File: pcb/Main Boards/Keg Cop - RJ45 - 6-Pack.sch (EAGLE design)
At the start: 25 parts

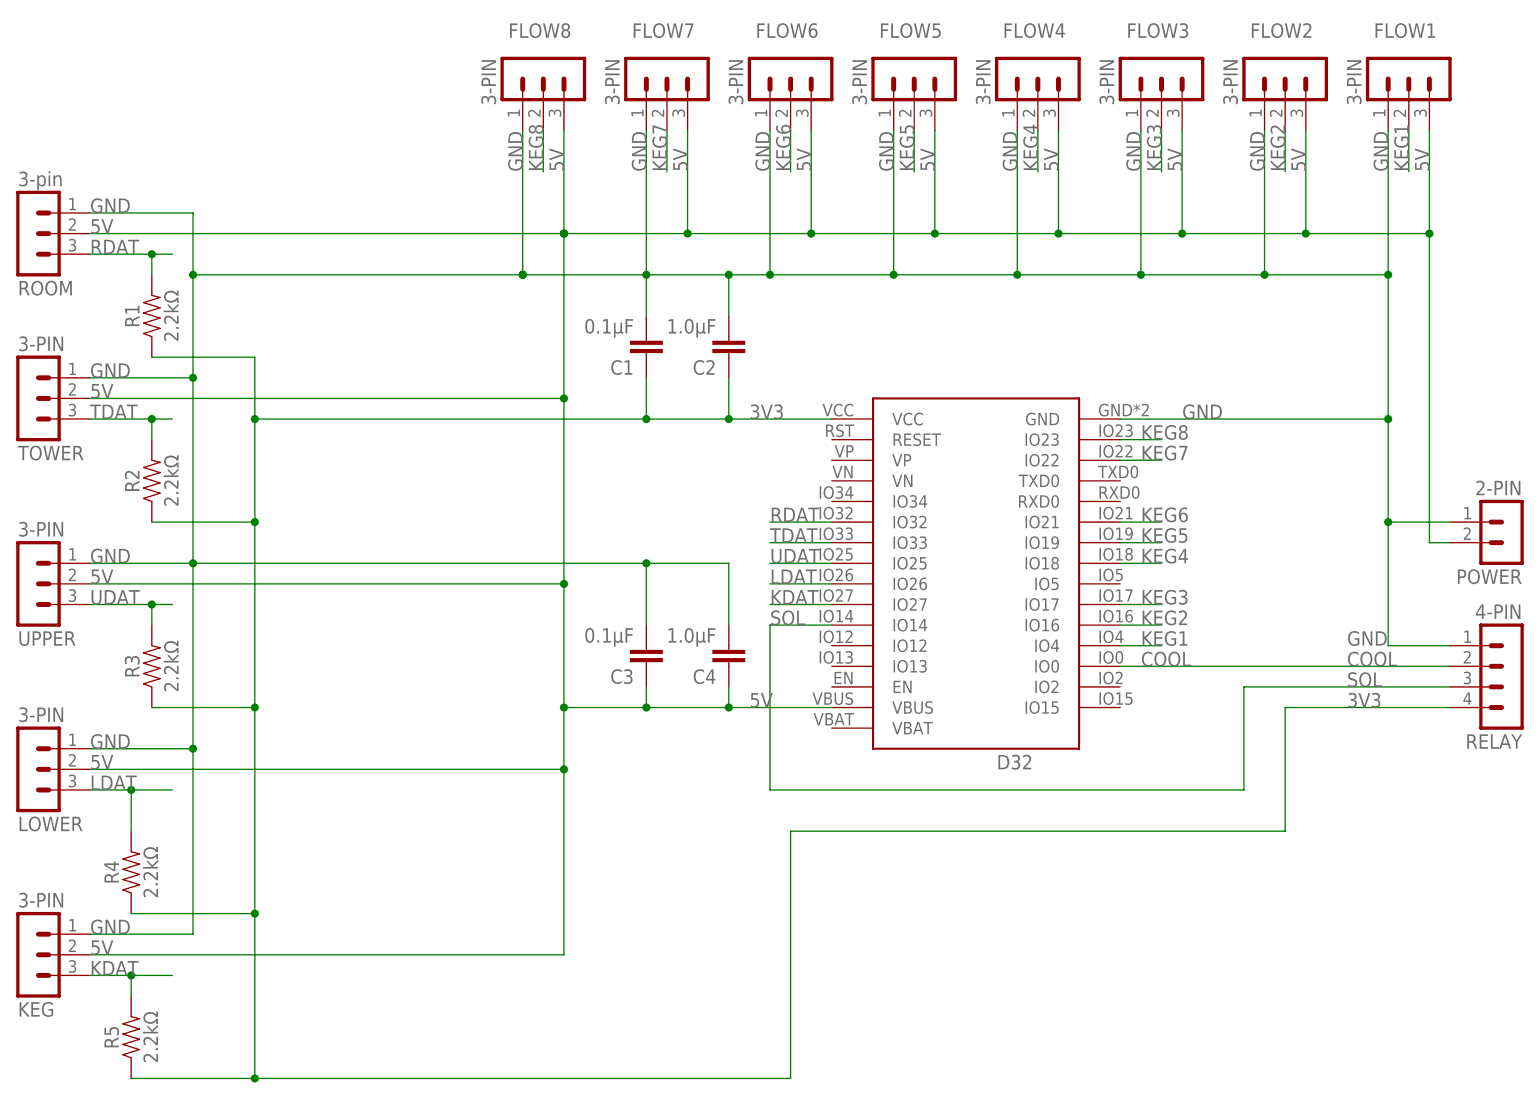
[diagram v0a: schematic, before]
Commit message: Swap pins, split dirs
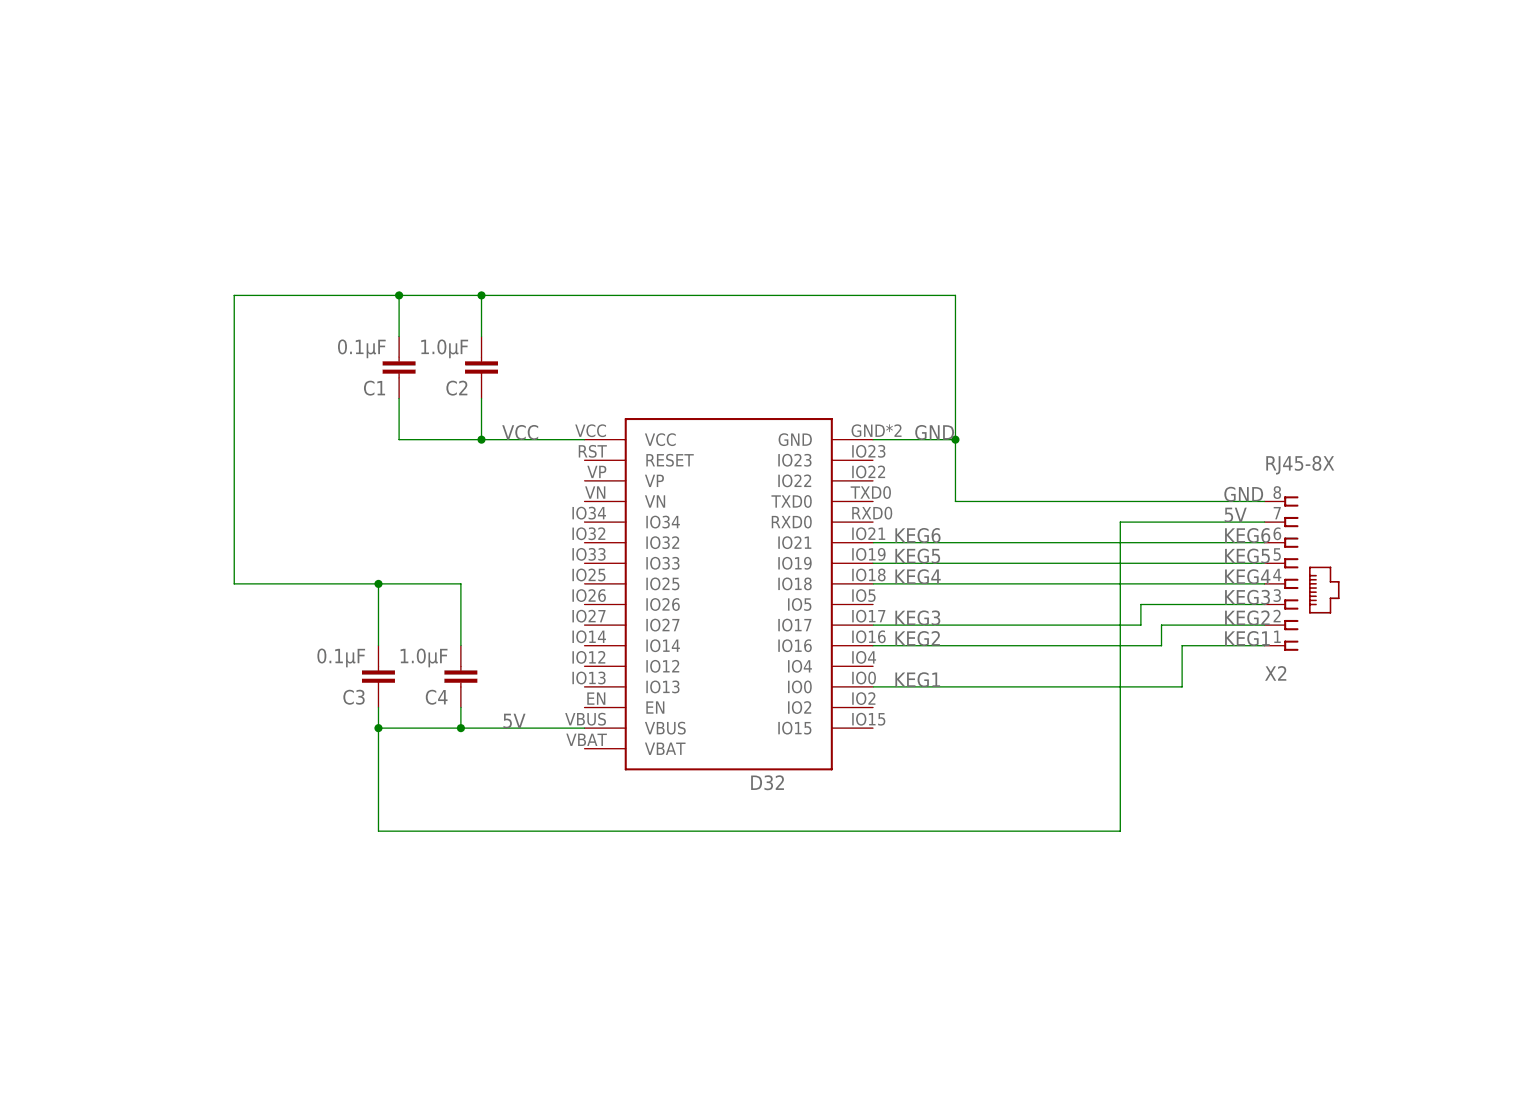
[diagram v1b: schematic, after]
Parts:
- removed FLOW1, FLOW2, FLOW3, FLOW4, FLOW5, FLOW6, FLOW7, FLOW8, KEG, LOWER, TOWER, UPPER: 3-PIN, Donnie:MA03-1
- removed POWER: 2-PIN, Donnie:HDR-2
- removed R1, R2, R3, R4, R5: 2.2kΩ, SparkFun-Resistors:RESISTORAXIAL-0.3
- removed RELAY: 4-PIN, Donnie:MA04-1
- removed ROOM: 3-pin, Donnie:MA03-1
- added X2: RJ45-8X, con-tycoelectronics:RJ45-8X
- D32: value (none) -> Lolin D32
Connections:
- removed net 3V3: C1.1, C2.1, D32.VCC, R1.1, R2.1, R3.1, R4.1, R5.1, RELAY.4
- removed net COOL: D32.IO0, RELAY.2
- removed net KDAT: D32.IO27, KEG.3, R5.2
- removed net KEG7: D32.IO22, FLOW7.2
- removed net KEG8: D32.IO23, FLOW8.2
- removed net LDAT: D32.IO26, LOWER.3, R4.2
- removed net RDAT: D32.IO32, R1.2, ROOM.3
- removed net SOL: D32.IO14, RELAY.3
- removed net TDAT: D32.IO33, R2.2, TOWER.3
- removed net UDAT: D32.IO25, R3.2, UPPER.3
- new net VCC: C1.1, C2.1, D32.VCC
- net 5V: now also X2.7; no longer FLOW1.3, FLOW2.3, FLOW3.3, FLOW4.3, FLOW5.3, FLOW6.3, FLOW7.3, FLOW8.3, KEG.2, LOWER.2, POWER.2, ROOM.2, TOWER.2, UPPER.2
- net GND: now also X2.8; no longer FLOW1.1, FLOW2.1, FLOW3.1, FLOW4.1, FLOW5.1, FLOW6.1, FLOW7.1, FLOW8.1, KEG.1, LOWER.1, POWER.1, RELAY.1, ROOM.1, TOWER.1, UPPER.1
- net KEG1: now also D32.IO0, X2.1; no longer D32.IO4, FLOW1.2
- net KEG2: now also X2.2; no longer FLOW2.2
- net KEG3: now also X2.3; no longer FLOW3.2
- net KEG4: now also X2.4; no longer FLOW4.2
- net KEG5: now also X2.5; no longer FLOW5.2
- net KEG6: now also X2.6; no longer FLOW6.2
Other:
- moved on the sheet: C1, C2, C3, C4, D32

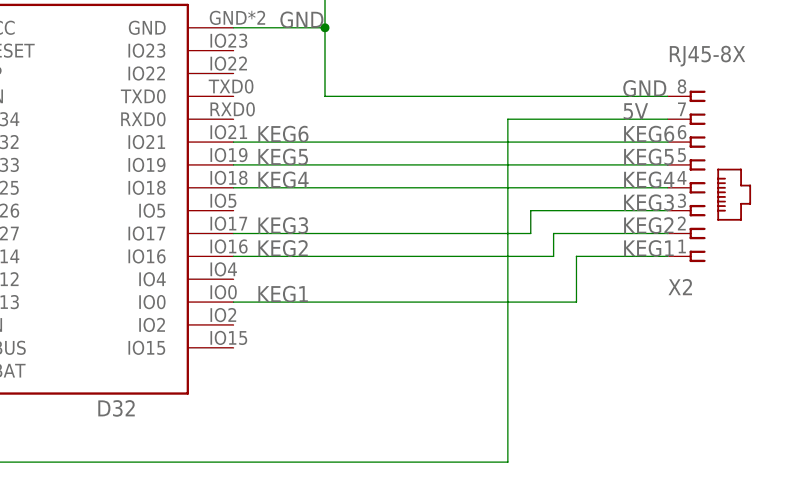
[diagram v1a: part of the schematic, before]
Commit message: Renamed files
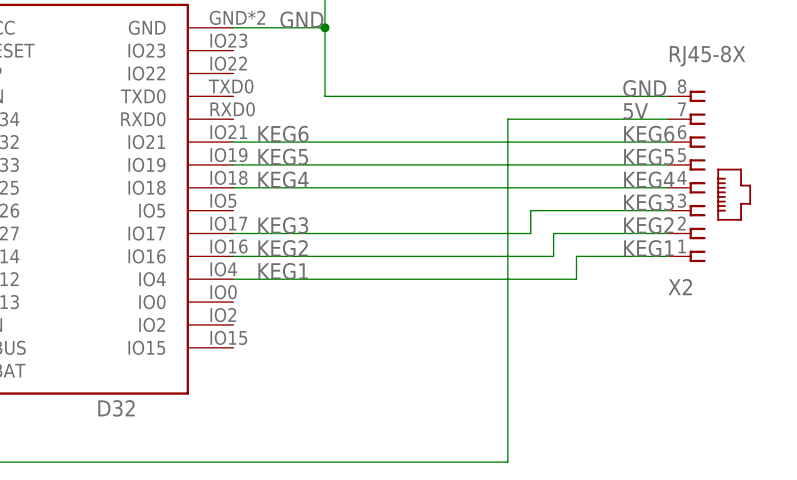
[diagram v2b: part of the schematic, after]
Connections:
- net KEG1: now also D32.IO4; no longer D32.IO0
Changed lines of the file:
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@@
 <label x="76.2" y="43.18" size="1.778" layer="95"/>
 <pinref part="X2" gate="G$1" pin="1"/>
-<pinref part="D32" gate="G$1" pin="IO0"/>
-<wire x1="33.02" y1="38.1" x2="71.12" y2="38.1" width="0.1524" layer="91"/>
-<wire x1="71.12" y1="38.1" x2="71.12" y2="43.18" width="0.1524" layer="91"/>
-<label x="35.56" y="38.1" size="1.778" layer="95"/>
+<pinref part="D32" gate="G$1" pin="IO4"/>
+<wire x1="33.02" y1="40.64" x2="71.12" y2="40.64" width="0.1524" layer="91"/>
+<wire x1="71.12" y1="40.64" x2="71.12" y2="43.18" width="0.1524" layer="91"/>
+<label x="35.56" y="40.64" size="1.778" layer="95"/>
 </segment>
 </net>
